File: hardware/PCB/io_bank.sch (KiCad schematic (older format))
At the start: 7 parts

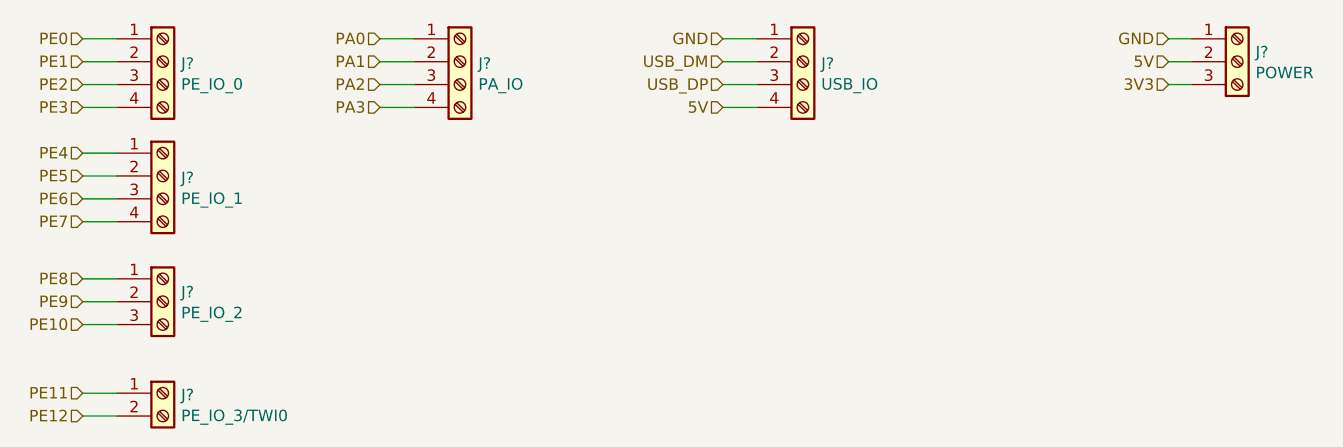
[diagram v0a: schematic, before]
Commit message: update rtl8723 circuit,
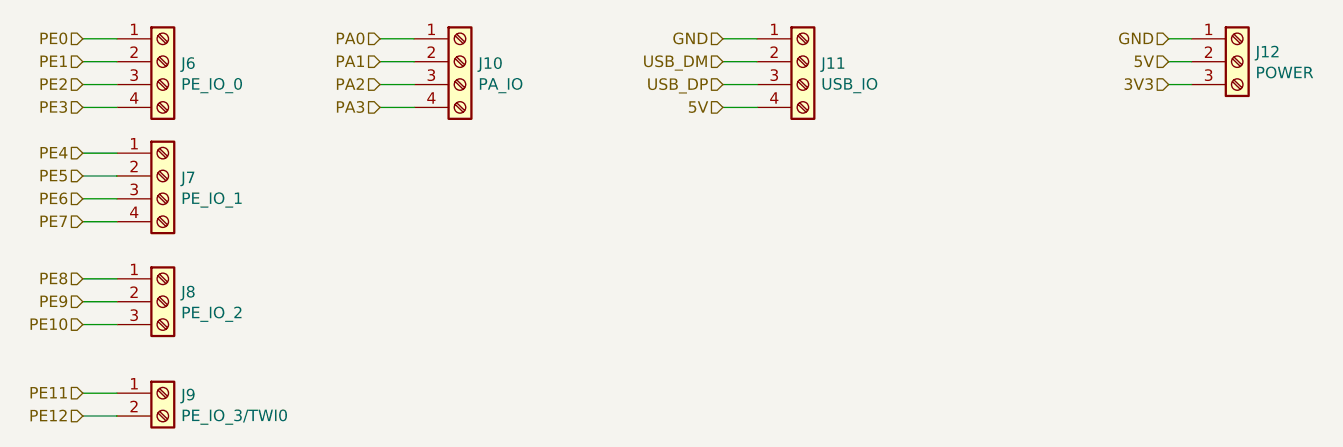
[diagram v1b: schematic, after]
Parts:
- J10, J11, J12, J6, J7, J8, J9: renamed from J?; footprint (none) -> Connector_PinHeader_2.54mm:PinHeader_1x04_P2.54mm_Vertical
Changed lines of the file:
@@
 $Descr A4 11693 8268
 encoding utf-8
-Sheet 6 6
+Sheet 5 6
 Title ""
 Date ""
@@
 3V3
 $Comp
-L Connector:Screw_Terminal_01x03 J?
+L Connector:Screw_Terminal_01x03 J12
 U 1 1 5EA42942
 P 6250 900
-F 0 "J?" H 6330 942 50  0000 L CNN
+F 0 "J12" H 6330 942 50  0000 L CNN
 F 1 "POWER" H 6330 851 50  0000 L CNN
-F 2 "" H 6250 900 50  0001 C CNN
+F 2 "Connector_PinHeader_2.54mm:PinHeader_1x04_P2.54mm_Vertical" H 6250 900 50  0001 C CNN
 F 3 "~" H 6250 900 50  0001 C CNN
 	1    6250 900
@@
 	5950 1000 6050 1000
 $Comp
-L Connector:Screw_Terminal_01x04 J?
+L Connector:Screw_Terminal_01x04 J11
 U 1 1 5EA44B19
 P 4350 900
-F 0 "J?" H 4430 892 50  0000 L CNN
+F 0 "J11" H 4430 892 50  0000 L CNN
 F 1 "USB_IO" H 4430 801 50  0000 L CNN
-F 2 "" H 4350 900 50  0001 C CNN
+F 2 "Connector_PinHeader_2.54mm:PinHeader_1x04_P2.54mm_Vertical" H 4350 900 50  0001 C CNN
 F 3 "~" H 4350 900 50  0001 C CNN
 	1    4350 900
@@
 	4000 1100 4150 1100
 $Comp
-L Connector:Screw_Terminal_01x04 J?
+L Connector:Screw_Terminal_01x04 J10
 U 1 1 5EA45B2D
 P 2850 900
-F 0 "J?" H 2930 892 50  0000 L CNN
+F 0 "J10" H 2930 892 50  0000 L CNN
 F 1 "PA_IO" H 2930 801 50  0000 L CNN
-F 2 "" H 2850 900 50  0001 C CNN
+F 2 "Connector_PinHeader_2.54mm:PinHeader_1x04_P2.54mm_Vertical" H 2850 900 50  0001 C CNN
 F 3 "~" H 2850 900 50  0001 C CNN
 	1    2850 900
@@
 PE5
 $Comp
-L Connector:Screw_Terminal_01x04 J?
+L Connector:Screw_Terminal_01x04 J6
 U 1 1 5EA4A367
 P 1550 900
-F 0 "J?" H 1630 892 50  0000 L CNN
+F 0 "J6" H 1630 892 50  0000 L CNN
 F 1 "PE_IO_0" H 1630 801 50  0000 L CNN
-F 2 "" H 1550 900 50  0001 C CNN
+F 2 "Connector_PinHeader_2.54mm:PinHeader_1x04_P2.54mm_Vertical" H 1550 900 50  0001 C CNN
 F 3 "~" H 1550 900 50  0001 C CNN
 	1    1550 900
@@
 	1200 1100 1350 1100
 $Comp
-L Connector:Screw_Terminal_01x04 J?
+L Connector:Screw_Terminal_01x04 J7
 U 1 1 5EA4BC4B
 P 1550 1400
-F 0 "J?" H 1630 1392 50  0000 L CNN
+F 0 "J7" H 1630 1392 50  0000 L CNN
 F 1 "PE_IO_1" H 1630 1301 50  0000 L CNN
-F 2 "" H 1550 1400 50  0001 C CNN
+F 2 "Connector_PinHeader_2.54mm:PinHeader_1x04_P2.54mm_Vertical" H 1550 1400 50  0001 C CNN
 F 3 "~" H 1550 1400 50  0001 C CNN
 	1    1550 1400
@@
 	1200 2050 1350 2050
 $Comp
-L Connector:Screw_Terminal_01x03 J?
+L Connector:Screw_Terminal_01x03 J8
 U 1 1 5EA4E4D8
 P 1550 1950
-F 0 "J?" H 1630 1992 50  0000 L CNN
+F 0 "J8" H 1630 1992 50  0000 L CNN
 F 1 "PE_IO_2" H 1630 1901 50  0000 L CNN
-F 2 "" H 1550 1950 50  0001 C CNN
+F 2 "Connector_PinHeader_2.54mm:PinHeader_1x04_P2.54mm_Vertical" H 1550 1950 50  0001 C CNN
 F 3 "~" H 1550 1950 50  0001 C CNN
 	1    1550 1950
@@
 $EndComp
 $Comp
-L Connector:Screw_Terminal_01x02 J?
+L Connector:Screw_Terminal_01x02 J9
 U 1 1 5EA4F4CE
 P 1550 2350
-F 0 "J?" H 1630 2342 50  0000 L CNN
+F 0 "J9" H 1630 2342 50  0000 L CNN
 F 1 "PE_IO_3/TWI0" H 1630 2251 50  0000 L CNN
-F 2 "" H 1550 2350 50  0001 C CNN
+F 2 "Connector_PinHeader_2.54mm:PinHeader_1x04_P2.54mm_Vertical" H 1550 2350 50  0001 C CNN
 F 3 "~" H 1550 2350 50  0001 C CNN
 	1    1550 2350

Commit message: update,
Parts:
- renumbered J12 to J10, J6 to J4, J7 to J5, J8 to J6, J9 to J7, J10 to J8, J11 to J9
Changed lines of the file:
@@
 $Descr A4 11693 8268
 encoding utf-8
-Sheet 5 6
+Sheet 4 6
 Title ""
 Date ""
@@
 3V3
 $Comp
-L Connector:Screw_Terminal_01x03 J12
+L Connector:Screw_Terminal_01x03 J10
 U 1 1 5EA42942
 P 6250 900
-F 0 "J12" H 6330 942 50  0000 L CNN
+F 0 "J10" H 6330 942 50  0000 L CNN
 F 1 "POWER" H 6330 851 50  0000 L CNN
 F 2 "Connector_PinHeader_2.54mm:PinHeader_1x04_P2.54mm_Vertical" H 6250 900 50  0001 C CNN
@@
 	5950 1000 6050 1000
 $Comp
-L Connector:Screw_Terminal_01x04 J11
+L Connector:Screw_Terminal_01x04 J9
 U 1 1 5EA44B19
 P 4350 900
-F 0 "J11" H 4430 892 50  0000 L CNN
+F 0 "J9" H 4430 892 50  0000 L CNN
 F 1 "USB_IO" H 4430 801 50  0000 L CNN
 F 2 "Connector_PinHeader_2.54mm:PinHeader_1x04_P2.54mm_Vertical" H 4350 900 50  0001 C CNN
@@
 	4000 1100 4150 1100
 $Comp
-L Connector:Screw_Terminal_01x04 J10
+L Connector:Screw_Terminal_01x04 J8
 U 1 1 5EA45B2D
 P 2850 900
-F 0 "J10" H 2930 892 50  0000 L CNN
+F 0 "J8" H 2930 892 50  0000 L CNN
 F 1 "PA_IO" H 2930 801 50  0000 L CNN
 F 2 "Connector_PinHeader_2.54mm:PinHeader_1x04_P2.54mm_Vertical" H 2850 900 50  0001 C CNN
@@
 PE5
 $Comp
-L Connector:Screw_Terminal_01x04 J6
+L Connector:Screw_Terminal_01x04 J4
 U 1 1 5EA4A367
 P 1550 900
-F 0 "J6" H 1630 892 50  0000 L CNN
+F 0 "J4" H 1630 892 50  0000 L CNN
 F 1 "PE_IO_0" H 1630 801 50  0000 L CNN
 F 2 "Connector_PinHeader_2.54mm:PinHeader_1x04_P2.54mm_Vertical" H 1550 900 50  0001 C CNN
@@
 	1200 1100 1350 1100
 $Comp
-L Connector:Screw_Terminal_01x04 J7
+L Connector:Screw_Terminal_01x04 J5
 U 1 1 5EA4BC4B
 P 1550 1400
-F 0 "J7" H 1630 1392 50  0000 L CNN
+F 0 "J5" H 1630 1392 50  0000 L CNN
 F 1 "PE_IO_1" H 1630 1301 50  0000 L CNN
 F 2 "Connector_PinHeader_2.54mm:PinHeader_1x04_P2.54mm_Vertical" H 1550 1400 50  0001 C CNN
@@
 	1200 2050 1350 2050
 $Comp
-L Connector:Screw_Terminal_01x03 J8
+L Connector:Screw_Terminal_01x03 J6
 U 1 1 5EA4E4D8
 P 1550 1950
-F 0 "J8" H 1630 1992 50  0000 L CNN
+F 0 "J6" H 1630 1992 50  0000 L CNN
 F 1 "PE_IO_2" H 1630 1901 50  0000 L CNN
 F 2 "Connector_PinHeader_2.54mm:PinHeader_1x04_P2.54mm_Vertical" H 1550 1950 50  0001 C CNN
@@
 $EndComp
 $Comp
-L Connector:Screw_Terminal_01x02 J9
+L Connector:Screw_Terminal_01x02 J7
 U 1 1 5EA4F4CE
 P 1550 2350
-F 0 "J9" H 1630 2342 50  0000 L CNN
+F 0 "J7" H 1630 2342 50  0000 L CNN
 F 1 "PE_IO_3/TWI0" H 1630 2251 50  0000 L CNN
 F 2 "Connector_PinHeader_2.54mm:PinHeader_1x04_P2.54mm_Vertical" H 1550 2350 50  0001 C CNN
